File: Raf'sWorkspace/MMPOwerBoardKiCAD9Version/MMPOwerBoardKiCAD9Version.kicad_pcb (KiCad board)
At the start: 2 copper layers, 79 x 60 mm, 103 parts, among them J1 TYPE-C-31-M-04, J2 Conn_02x16_Odd_Even, J3 Conn_01x02, Q1 SS8050, SW1 SS-12D11-G050, U1 HUSB237, U10 TPS22917DBVR, U11 AMS1117-5.0, U2 TP4056-42-ESOP8, U3 DRV8833PWPR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

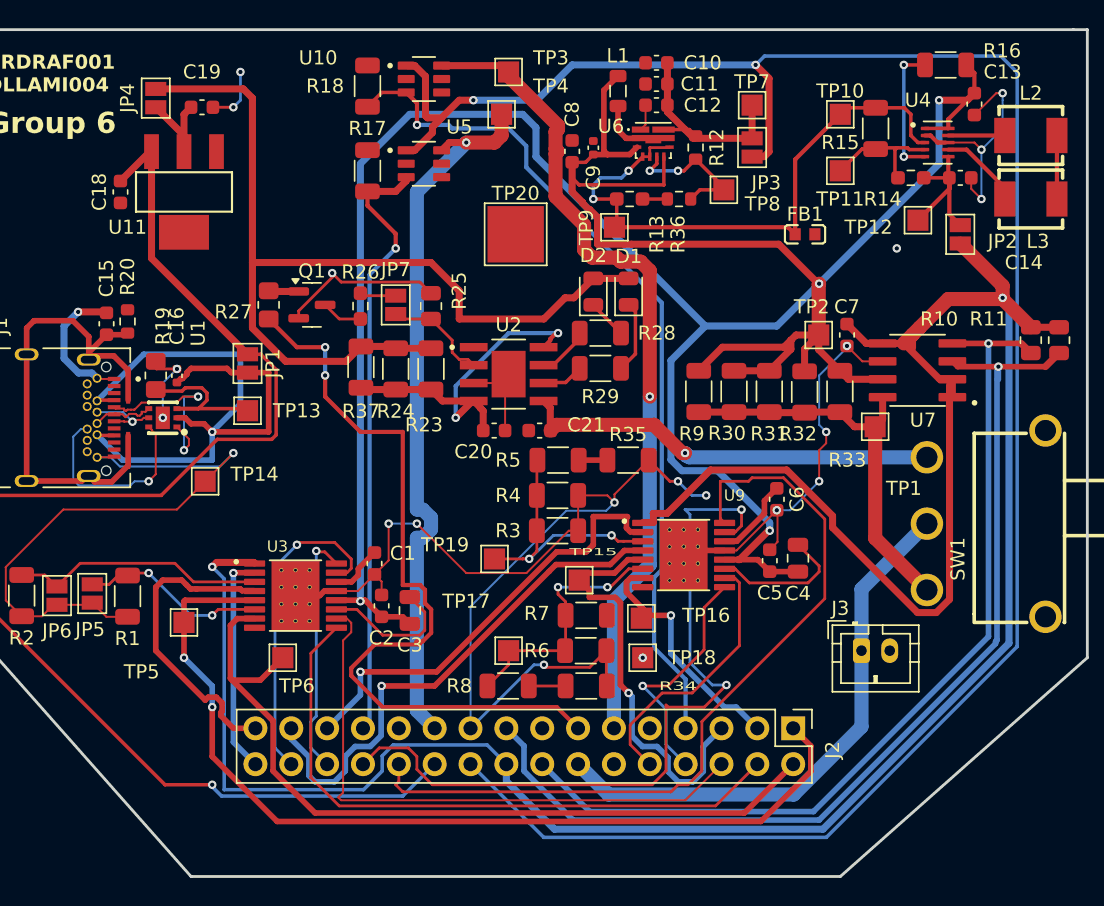
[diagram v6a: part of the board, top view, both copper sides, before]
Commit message: Made changes to hole sizes, minimum track width stuff (1.5mm) and other compliance things
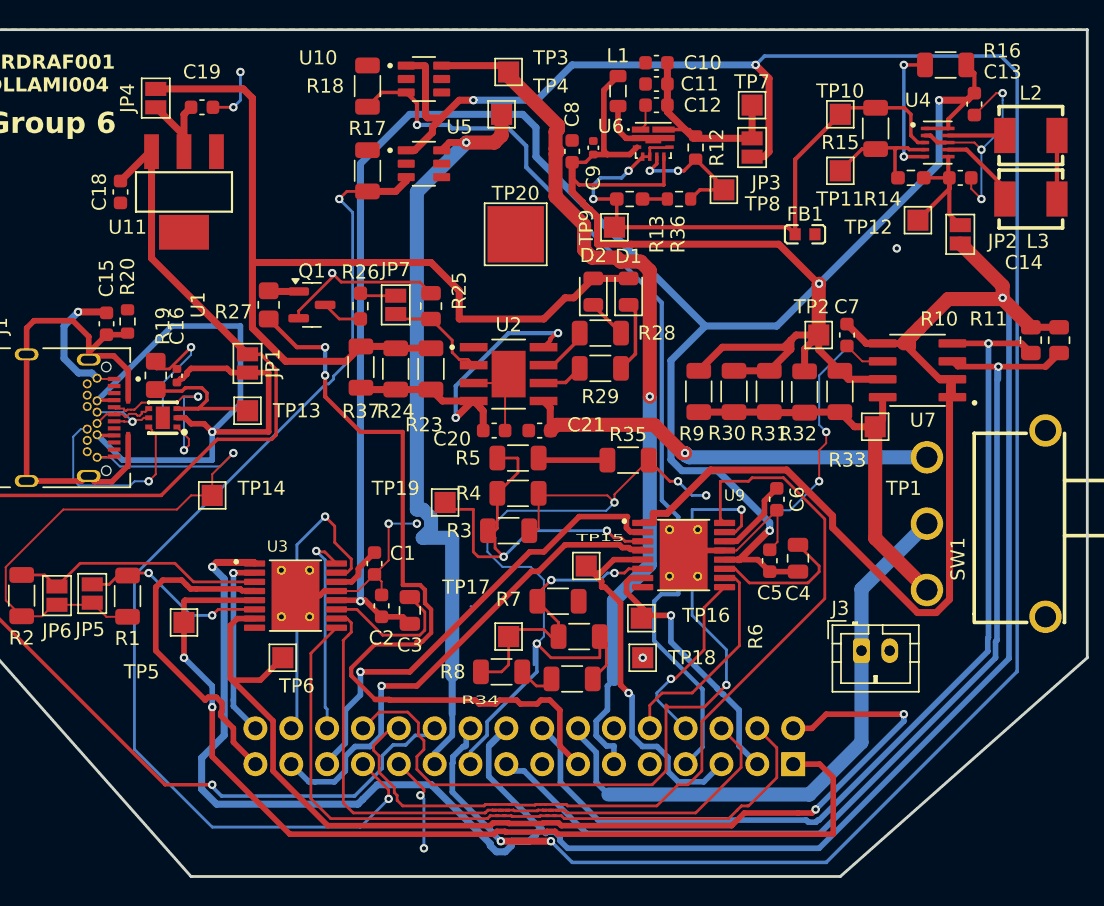
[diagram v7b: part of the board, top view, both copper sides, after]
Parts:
- J2: moved to B.Cu
- moved TP19 5.32 mm to (198.0, 82.5)
- moved R3 3.46 mm to (202.5, 84.5)
- moved R5 2.84 mm to (203.2, 79.4)
- moved R4 2.80 mm to (203.2, 81.9)
- moved J2 2.54 mm to (222.7, 101.0), turned to 90 degrees
- moved R7 2.24 mm to (206.0, 89.5)
- moved R34 1.12 mm to (207.0, 95.0)
- moved TP14 1.12 mm to (181.5, 82.0)
- moved TP15 1.12 mm to (208.0, 87.0)
- moved R6 1.10 mm to (207.5, 92.0)
- moved R8 1.10 mm to (202.0, 94.5)
- moved TP17 1.00 mm to (202.5, 92.0)
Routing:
- net /EXT_LOAD1_CTRL: track 43.1 -> 75.8 mm, vias 1 -> 2
- net /Motor2_A_OUT: track 57.2 -> 76.0 mm, vias 0 -> 2
- net /3V3: track 183.7 -> 195.9 mm
- net Net-(U9-AISEN): track 18.3 -> 28.5 mm
- net /5V: track 148.4 -> 156.5 mm, vias 2 -> 4
- net GND: track 208.7 -> 216.0 mm, vias 22 -> 21
- net /MOTOR2_CTRL1: track 45.1 -> 51.9 mm
- net /MOTOR3_CTRL1: track 57.3 -> 63.0 mm
- net /MOTOR2_CTRL2: track 42.2 -> 47.6 mm
- net /EXT_LOAD2_CTRL: track 60.5 -> 65.7 mm
- net /Motor2_B_OUT: track 66.2 -> 70.6 mm
- net /MOTOR4_CTRL1: track 17.2 -> 13.0 mm
- net /EXT_LOAD1_OUT: track 51.0 -> 55.2 mm
- net /EXT_LOAD2_OUT: track 58.8 -> 62.7 mm
- net /I2C1_SCL: track 64.8 -> 68.5 mm
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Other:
- board text added: "Need to check: If we make whole size's 3mm and increase diameters, it that fine?"
- board text added: "Problem seems to be H-bridges thermal vias... what about USB-C and normal Vias"

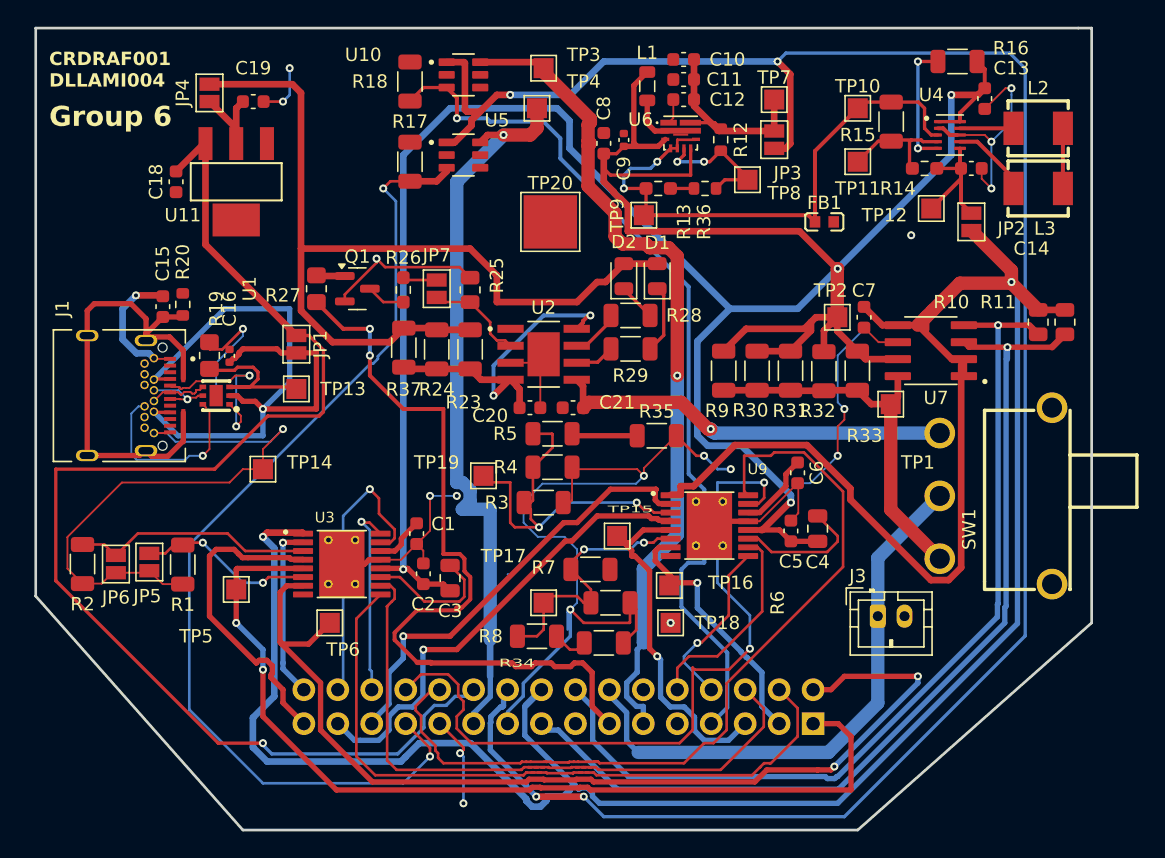
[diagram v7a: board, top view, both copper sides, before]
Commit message: Changed the USB-C connector, and connected it - removed Ground layers, changed silkscreens for a few units
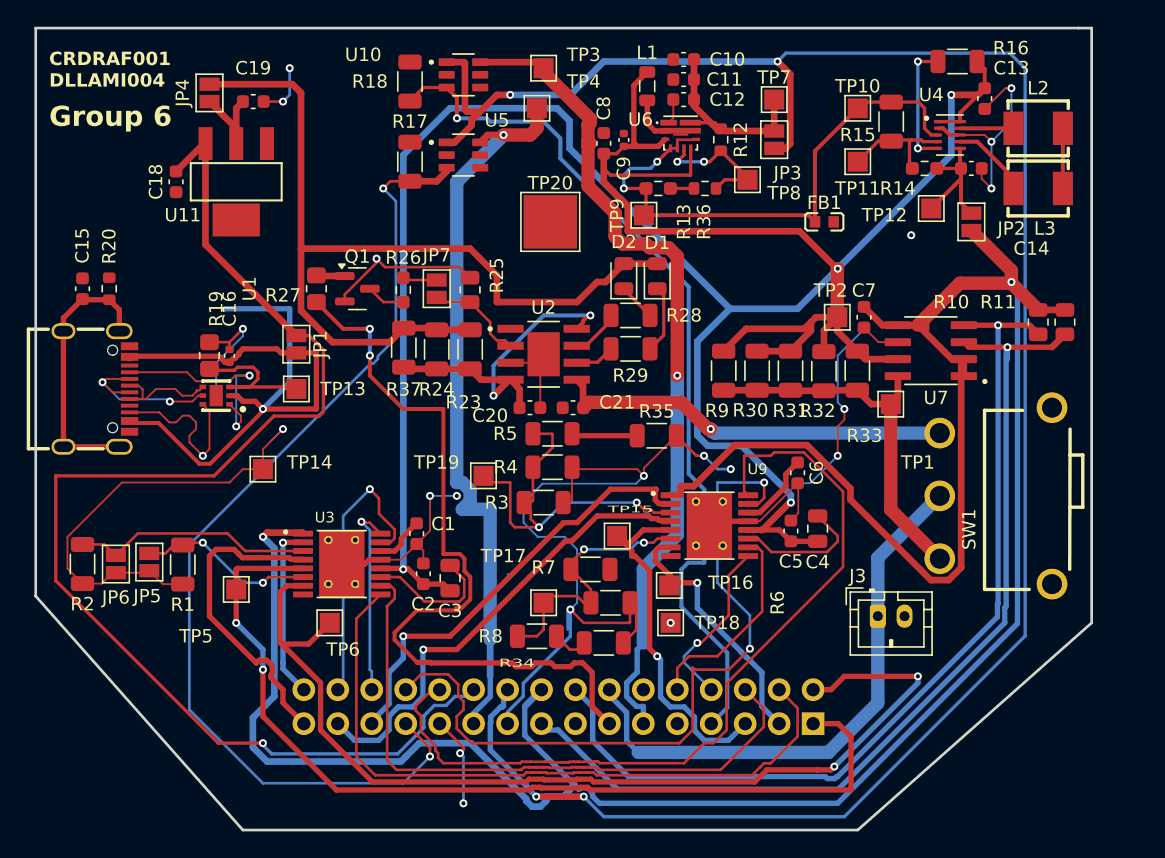
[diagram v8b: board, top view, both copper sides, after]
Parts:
- J1: footprint TYPE-C-31-M-04:HRO_TYPE-C-31-M-04 -> TYPE-C-31-M-04:USB-C_SMD-TYPE-C-31-M-12
- moved C15 6.16 mm to (168.0, 68.5)
- moved R20 5.62 mm to (170.0, 68.5)
- moved J1 5.53 mm to (169.0, 76.0)
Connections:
- J1 pad S3: Net-(C15-Pad1) -> (no net)
- J1 pad S4: Net-(C15-Pad1) -> (no net)
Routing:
- net GND: track 216.0 -> 195.5 mm, vias 21 -> 20
- net Net-(C15-Pad1): track 36.9 -> 20.5 mm
- net Net-(J1-DN1): track 5.36 -> 12.7 mm, vias 1 -> 2
- net Net-(J1-DP1): track 4.60 -> 8.13 mm
- net Net-(J1-CC1): track 13.5 -> 16.4 mm
- net Net-(J1-CC2): track 14.3 -> 13.2 mm
- removed copper zone on B.Cu, net GND
- removed copper zone on F.Cu, net GND
